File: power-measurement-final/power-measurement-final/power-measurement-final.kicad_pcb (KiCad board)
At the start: 4 copper layers, 89 x 89 mm, 76 parts, among them J1 Screw_Terminal_01x04, J10 Conn_01x01_Pin, J11 Conn_01x02_Pin, J12 Conn_01x01_Pin, J13 Conn_01x01_Pin, J2 Conn_01x02_Socket, J3 Conn_01x03_Socket, J4 Conn_01x07_Socket, J5 Conn_01x07_Socket, J6 Conn_01x05_Socket, J7 RFShield_OnePiece, J8 Conn_01x03_Socket, J9 Conn_01x01_Pin, U1 MCP3911A0-E-SS, U2 Si8641BA-B-IU, U4 LM317_TO-252, U6 ADuM1250, Y1 10M

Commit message: updates
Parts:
- removed R22: 10k, Potentiometer_THT:Potentiometer_ACP_CA9-V10_Vertical_Hole
- added RV2: R_Potentiometer, Potentiometer_THT:Potentiometer_ACP_CA9-V10_Vertical_Hole, F.Cu at (153.3, 94.5)
- moved R25 3.39 mm to (175.0, 120.0), turned to 90 degrees
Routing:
- net GNDD: track 117.8 -> 174.4 mm, vias 0 -> 2
- net +5V: track 247.0 -> 221.6 mm
- net /SDA/XCK/PB1: track 3.80 -> 8.47 mm
- net Net-(J11-Pin_2): track 10.6 -> 6.14 mm

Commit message: power rmeasurement final finished
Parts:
- added D5: D_Zener_Small, Diode_SMD:D_1206_3216Metric_Pad1.42x1.75mm_HandSolder, B.Cu at (106.6, 133.6)
- added TP4: TestPoint, TestPoint:TestPoint_Plated_Hole_D3.0mm, F.Cu at (100.3, 143.8)
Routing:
- net +5V: track 221.6 -> 224.9 mm
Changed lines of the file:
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@@
   (net 65 "unconnected-(RV2-Pad3)")
   (net 66 "Net-(R27-Pad2)")
+  (net 67 "unconnected-(TP4-Pad1)")
   (footprint "Connector_PinHeader_2.54mm:PinHeader_1x01_P2.54mm_Vertical" (layer "F.Cu")
     (at 177.927 109.4994)
@@
     )
   )
+  (footprint "TestPoint:TestPoint_Plated_Hole_D3.0mm" (layer "F.Cu")
+    (at 100.3 143.8)
+    (descr "Plated Hole as test Point, diameter 3.0mm")
+    (tags "test point plated hole")
+    (property "Sheetfile" "power-measurement-final.kicad_sch")
+    (property "Sheetname" "")
+    (property "ki_description" "test point")
+    (property "ki_keywords" "test point tp")
+    (attr exclude_from_pos_files)
+    (fp_text reference "TP4" (at 0 -3.048) (layer "F.SilkS")
+        (effects (font (size 1 1) (thickness 0.15)))
+    )
+    (fp_text value "TestPoint" (at 0 3) (layer "F.Fab")
+        (effects (font (size 1 1) (thickness 0.15)))
+    )
+    (fp_text user "${REFERENCE}" (at 0 -3.05) (layer "F.Fab")
+        (effects (font (size 1 1) (thickness 0.15)))
+    )
+    (fp_circle (center 0 0) (end 0 -2.286)
+      (stroke (width 0.12) (type solid)) (fill none) (layer "F.SilkS"))
+    (fp_circle (center 0 0) (end 2.5 0)
+      (stroke (width 0.05) (type solid)) (fill none) (layer "F.CrtYd"))
+    (pad "1" thru_hole circle (at 0 0) (size 4 4) (drill 3) (layers "*.Cu" "*.Mask")
+      (net 67 "unconnected-(TP4-Pad1)") (pinfunction "1") (pintype "passive+no_connect"))
+  )
   (footprint "Connector_PinSocket_2.54mm:PinSocket_1x03_P2.54mm_Vertical" (layer "F.Cu")
     (at 161.71465 125.23666 180)
@@
     )
   )
+  (footprint "Diode_SMD:D_1206_3216Metric_Pad1.42x1.75mm_HandSolder" (layer "B.Cu")
+    (at 106.6 133.6)
+    (descr "Diode SMD 1206 (3216 Metric), square (rectangular) end terminal, IPC_7351 nominal, (Body size source: http://www.tortai-tech.com/upload/download/2011102023233369053.pdf), generated with kicad-footprint-generator")
+    (tags "diode handsolder")
+    (property "Sheetfile" "power-measurement-final.kicad_sch")
+    (property "Sheetname" "")
+    (property "ki_description" "Zener diode, small symbol")
+    (property "ki_keywords" "diode")
+    (attr smd)
+    (fp_text reference "D5" (at 0 1.82) (layer "B.SilkS")
+        (effects (font (size 1 1) (thickness 0.15)) (justify mirror))
+    )
+    (fp_text value "D_Zener_Small" (at 0 -1.82) (layer "B.Fab")
+        (effects (font (size 1 1) (thickness 0.15)) (justify mirror))
+    )
+    (fp_text user "${REFERENCE}" (at 0 0) (layer "B.Fab")
+        (effects (font (size 0.8 0.8) (thickness 0.12)) (justify mirror))
+    )
+    (fp_line (start -2.46 -1.135) (end 1.6 -1.135)
+      (stroke (width 0.12) (type solid)) (layer "B.SilkS"))
+    (fp_line (start -2.46 1.135) (end -2.46 -1.135)
+      (stroke (width 0.12) (type solid)) (layer "B.SilkS"))
+    (fp_line (start 1.6 1.135) (end -2.46 1.135)
+      (stroke (width 0.12) (type solid)) (layer "B.SilkS"))
+    (fp_line (start -2.45 -1.12) (end -2.45 1.12)
+      (stroke (width 0.05) (type solid)) (layer "B.CrtYd"))
+    (fp_line (start -2.45 1.12) (end 2.45 1.12)
+      (stroke (width 0.05) (type solid)) (layer "B.CrtYd"))
+    (fp_line (start 2.45 -1.12) (end -2.45 -1.12)
+      (stroke (width 0.05) (type solid)) (layer "B.CrtYd"))
+    (fp_line (start 2.45 1.12) (end 2.45 -1.12)
+      (stroke (width 0.05) (type solid)) (layer "B.CrtYd"))
+    (fp_line (start -1.6 -0.8) (end 1.6 -0.8)
+      (stroke (width 0.1) (type solid)) (layer "B.Fab"))
+    (fp_line (start -1.6 0.4) (end -1.6 -0.8)
+      (stroke (width 0.1) (type solid)) (layer "B.Fab"))
+    (fp_line (start -1.2 0.8) (end -1.6 0.4)
+      (stroke (width 0.1) (type solid)) (layer "B.Fab"))
+    (fp_line (start 1.6 -0.8) (end 1.6 0.8)
+      (stroke (width 0.1) (type solid)) (layer "B.Fab"))
+    (fp_line (start 1.6 0.8) (end -1.2 0.8)
+      (stroke (width 0.1) (type solid)) (layer "B.Fab"))
+    (pad "1" smd roundrect (at -1.4875 0) (size 1.425 1.75) (layers "B.Cu" "B.Paste" "B.Mask") (roundrect_rratio 0.175439)
+      (net 47 "+5V") (pinfunction "K") (pintype "passive"))
+    (pad "2" smd roundrect (at 1.4875 0) (size 1.425 1.75) (layers "B.Cu" "B.Paste" "B.Mask") (roundrect_rratio 0.175439)
+      (net 19 "GND") (pinfunction "A") (pintype "passive"))
+    (model "${KICAD6_3DMODEL_DIR}/Diode_SMD.3dshapes/D_1206_3216Metric.wrl"
+      (offset (xyz 0 0 0))
+      (scale (xyz 1 1 1))
+      (rotate (xyz 0 0 0))
+    )
+  )
   (footprint "Capacitor_SMD:C_1206_3216Metric_Pad1.33x1.80mm_HandSolder" (layer "B.Cu")
     (at 136.525 92.71 180)
@@
   (segment (start 132.36 108.466882) (end 132.3594 108.466282) (width 0.5) (layer "B.Cu") (net 47))
   (segment (start 114.5286 130.5552) (end 116.7646 130.5552) (width 1) (layer "B.Cu") (net 47))
+  (segment (start 102.3353 132.3353) (end 104.1154 130.5552) (width 1) (layer "B.Cu") (net 47))
   (segment (start 184.6 139.05) (end 185.25 138.4) (width 1) (layer "B.Cu") (net 47))
   (segment (start 124.395712 112.506835) (end 124.395712 112.559312) (width 0.4) (layer "B.Cu") (net 47))
@@
   (segment (start 127.65465 121.73666) (end 127.61465 121.69666) (width 1) (layer "B.Cu") (net 47))
   (segment (start 139.954 111.506) (end 139.928 111.48) (width 0.5) (layer "B.Cu") (net 47))
-  (segment (start 100.2284 134.4422) (end 104.1154 130.5552) (width 1) (layer "B.Cu") (net 47))
+  (segment (start 103.6 133.6) (end 105.1125 133.6) (width 1) (layer "B.Cu") (net 47))
   (segment (start 147.5486 111.5054) (end 147.5486 116.0272) (width 1) (layer "B.Cu") (net 47))
   (segment (start 140.5412 106.6008) (end 140.7545 106.3875) (width 0.5) (layer "B.Cu") (net 47))
@@
   (segment (start 147.5486 116.0272) (end 141.83914 121.73666) (width 1) (layer "B.Cu") (net 47))
   (segment (start 181.9017 106.3875) (end 148.5646 106.3875) (width 1) (layer "B.Cu") (net 47))
+  (segment (start 100.2284 134.4422) (end 102.3353 132.3353) (width 1) (layer "B.Cu") (net 47))
   (segment (start 183.9849 108.4961) (end 182.7149 108.4961) (width 1) (layer "B.Cu") (net 47))
   (segment (start 184.5176 116.6876) (end 185.26 115.9452) (width 1) (layer "B.Cu") (net 47))
@@
   (segment (start 171.577 142.533) (end 171.577 128.524) (width 1) (layer "B.Cu") (net 47))
   (segment (start 104.1154 130.5552) (end 111.1786 130.5552) (width 1) (layer "B.Cu") (net 47))
+  (segment (start 102.3353 132.3353) (end 103.6 133.6) (width 1) (layer "B.Cu") (net 47))
   (segment (start 125.62314 121.69666) (end 127.61465 121.69666) (width 1) (layer "B.Cu") (net 47))
   (segment (start 133.98 111.48) (end 132.36 109.86) (width 0.5) (layer "B.Cu") (net 47))

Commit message: ...
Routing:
- net HIGH_in: track 200.7 -> 191.8 mm
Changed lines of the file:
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@@
   (segment (start 178.0032 88.392) (end 176.1744 90.2208) (width 2) (layer "B.Cu") (net 45))
   (segment (start 101.2444 91.4292) (end 105.6024 91.4292) (width 2) (layer "B.Cu") (net 45))
-  (segment (start 99.2124 66.413084) (end 106.725484 58.9) (width 2) (layer "B.Cu") (net 45))
+  (segment (start 107.5 59.2) (end 165.5 59.2) (width 2) (layer "B.Cu") (net 45))
   (segment (start 174.701 95.7074) (end 174.7012 95.7072) (width 1) (layer "B.Cu") (net 45))
+  (segment (start 99.2124 67.4876) (end 107.5 59.2) (width 2) (layer "B.Cu") (net 45))
   (segment (start 176.022 73.787) (end 176.911 74.676) (width 2) (layer "B.Cu") (net 45))
   (segment (start 183.642 73.66) (end 183.642 66.294) (width 2) (layer "B.Cu") (net 45))
-  (segment (start 106.725484 58.9) (end 174.47 58.9) (width 2) (layer "B.Cu") (net 45))
   (segment (start 107.442 93.2688) (end 107.442 98.3996) (width 2) (layer "B.Cu") (net 45))
-  (segment (start 182.626 74.676) (end 183.642 73.66) (width 2) (layer "B.Cu") (net 45))
   (segment (start 176.1744 94.234) (end 174.7012 95.7072) (width 2) (layer "B.Cu") (net 45))
-  (segment (start 183.642 66.294) (end 177.546 60.198) (width 2) (layer "B.Cu") (net 45))
+  (segment (start 101.2444 91.4292) (end 99.2124 89.3972) (width 2) (layer "B.Cu") (net 45))
+  (segment (start 177.546 60.198) (end 167.64 60.198) (width 2) (layer "B.Cu") (net 45))
   (segment (start 176.022 77.343) (end 176.022 73.787) (width 3) (layer "B.Cu") (net 45))
   (segment (start 105.6024 91.4292) (end 107.442 93.2688) (width 2) (layer "B.Cu") (net 45))
   (segment (start 178.308 74.549) (end 176.022 72.263) (width 2) (layer "B.Cu") (net 45))
-  (segment (start 99.2124 89.3972) (end 99.2124 66.413084) (width 2) (layer "B.Cu") (net 45))
   (segment (start 183.642 75.692) (end 183.642 87.376) (width 2) (layer "B.Cu") (net 45))
   (segment (start 178.308 74.676) (end 182.626 74.676) (width 2) (layer "B.Cu") (net 45))
   (segment (start 171.1706 95.7074) (end 174.701 95.7074) (width 1) (layer "B.Cu") (net 45))
-  (segment (start 101.2444 91.4292) (end 99.2124 89.3972) (width 2) (layer "B.Cu") (net 45))
+  (segment (start 165.5 59.2) (end 166.37 60.07) (width 2) (layer "B.Cu") (net 45))
   (segment (start 178.308 75.057) (end 176.022 77.343) (width 2) (layer "B.Cu") (net 45))
+  (segment (start 167.64 60.198) (end 166.37 61.468) (width 2) (layer "B.Cu") (net 45))
   (segment (start 176.1744 90.2208) (end 176.1744 94.234) (width 2) (layer "B.Cu") (net 45))
-  (segment (start 174.498 61.468) (end 166.37 61.468) (width 2) (layer "B.Cu") (net 45))
-  (segment (start 175.768 60.198) (end 174.498 61.468) (width 2) (layer "B.Cu") (net 45))
+  (segment (start 182.626 74.676) (end 183.642 73.66) (width 2) (layer "B.Cu") (net 45))
   (segment (start 176.022 75.565) (end 176.022 77.343) (width 2) (layer "B.Cu") (net 45))
   (segment (start 176.022 73.787) (end 176.022 72.263) (width 3) (layer "B.Cu") (net 45))
+  (segment (start 183.642 66.294) (end 177.546 60.198) (width 2) (layer "B.Cu") (net 45))
   (segment (start 182.626 88.392) (end 178.0032 88.392) (width 2) (layer "B.Cu") (net 45))
   (segment (start 182.626 74.676) (end 183.642 75.692) (width 2) (layer "B.Cu") (net 45))
   (segment (start 183.642 87.376) (end 182.626 88.392) (width 2) (layer "B.Cu") (net 45))
   (segment (start 178.308 74.676) (end 178.308 75.057) (width 2) (layer "B.Cu") (net 45))
+  (segment (start 166.37 60.07) (end 166.37 61.468) (width 2) (layer "B.Cu") (net 45))
   (segment (start 178.308 74.676) (end 178.308 74.549) (width 2) (layer "B.Cu") (net 45))
-  (segment (start 177.546 60.198) (end 175.768 60.198) (width 2) (layer "B.Cu") (net 45))
+  (segment (start 99.2124 89.3972) (end 99.2124 67.4876) (width 2) (layer "B.Cu") (net 45))
   (segment (start 176.911 74.676) (end 176.022 75.565) (width 2) (layer "B.Cu") (net 45))
   (segment (start 176.911 74.676) (end 178.308 74.676) (width 2) (layer "B.Cu") (net 45))
-  (segment (start 174.47 58.9) (end 175.768 60.198) (width 2) (layer "B.Cu") (net 45))
   (segment (start 122.5042 94.107) (end 122.5042 97.6122) (width 0.4) (layer "In2.Cu") (net 46))
   (segment (start 116.3066 103.8098) (end 116.3066 108.0008) (width 0.4) (layer "In2.Cu") (net 46))

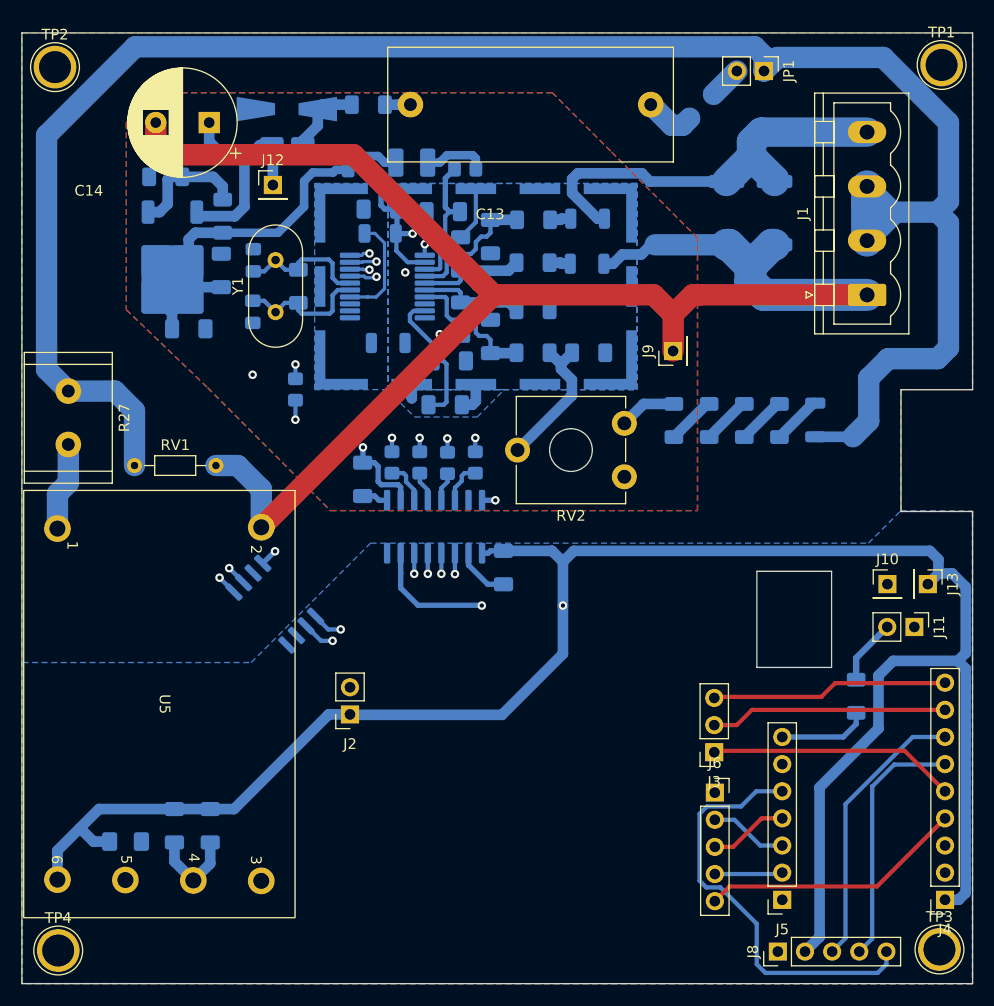
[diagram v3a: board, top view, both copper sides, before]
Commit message: Updated power measurement
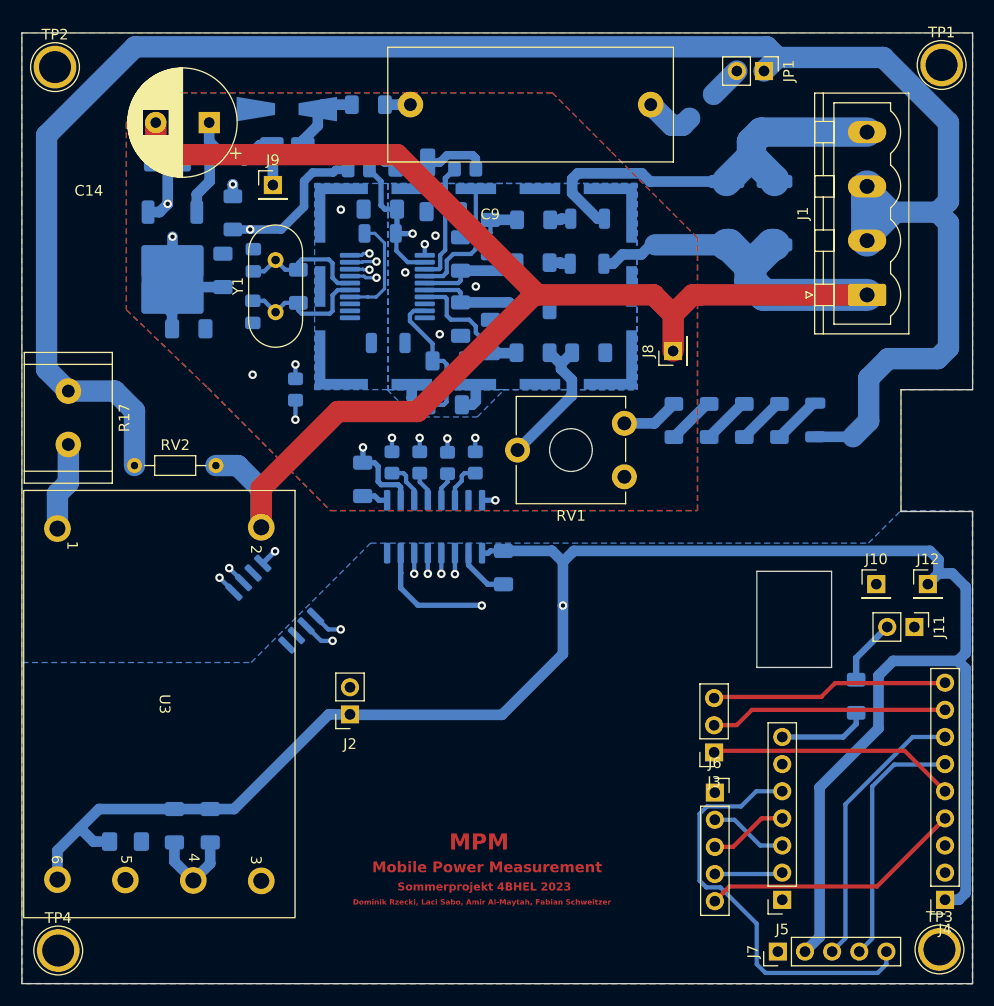
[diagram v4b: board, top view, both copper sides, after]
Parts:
- removed the J13 at (181.7, 109.5)
- added J12: Conn_01x01_Pin, Connector_PinHeader_2.54mm:PinHeader_1x01_P2.54mm_Vertical, F.Cu at (181.7, 109.5)
- moved R22 1.38 mm to (110.5, 70.0)
- moved J10 1.04 mm to (176.9, 109.5)
- moved R23 1.00 mm to (116.7, 74.8)
- moved C18 0.15 mm to (115.7, 80.1)
- renumbered C5 to C1, C2 to C10, C1 to C11, C4 to C12, C17 to C13, C3 to C15, C18 to C16, C15 to C17, C16 to C18, C11 to C2, C12 to C3, C10 to C4, C6 to C5, C7 to C6, C8 to C7, C9 to C8, C13 to C9, D5 to D3, J7 to J13, J8 to J7, J9 to J8, J12 to J9, L5 to L1, L1 to L5, R15 to R1, R21 to R10, R14 to R11, R8 to R12, R9 to R13, R10 to R14, R11 to R15, R12 to R16, R27 to R17, R17 to R18, R1 to R19, R16 to R2, R2 to R20, R3 to R21, R23 to R22, R24 to R23, R26 to R24, R4 to R3, R5 to R4, R6 to R5, R7 to R6, R18 to R7, R19 to R8, R20 to R9, RV2 to RV1, RV1 to RV2, U5 to U3, U6 to U5
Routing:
- net GNDD: track 174.4 -> 180.7 mm, vias 2 -> 3
- net +3.3V: track 33.9 -> 39.0 mm, vias 0 -> 2
- net Net-(U4-ADJ): track 11.3 -> 15.3 mm, vias 0 -> 2
- net /LM317_input: track 22.1 -> 19.2 mm
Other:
- board text added: "Dominik Rzecki, Laci Sabo, Amir Al-Maytah, Fabian Schweitzer"
- board text added: "MPM"
- board text added: "Mobile Power Measurement"
- board text added: "Sommerprojekt 4BHEL 2023"
